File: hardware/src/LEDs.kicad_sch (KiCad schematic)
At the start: 0 parts

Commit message: Add: LEDs to the schematic
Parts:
- added R601: 220R, symbol Device:R
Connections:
- new net LED11-1/D_{IN}: R601.1
- new net LED_{IN}: R601.2
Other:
- added sheet LED11-1 (LEDx11.kicad_sch)
- added sheet LED11-10 (LEDx11.kicad_sch)
- added sheet LED11-2 (LEDx11.kicad_sch)
- added sheet LED11-3 (LEDx11.kicad_sch)
- added sheet LED11-4 (LEDx11.kicad_sch)
- added sheet LED11-5 (LEDx11.kicad_sch)
- added sheet LED11-6 (LEDx11.kicad_sch)
- added sheet LED11-7 (LEDx11.kicad_sch)
- added sheet LED11-8 (LEDx11.kicad_sch)
- added sheet LED11-9 (LEDx11.kicad_sch)

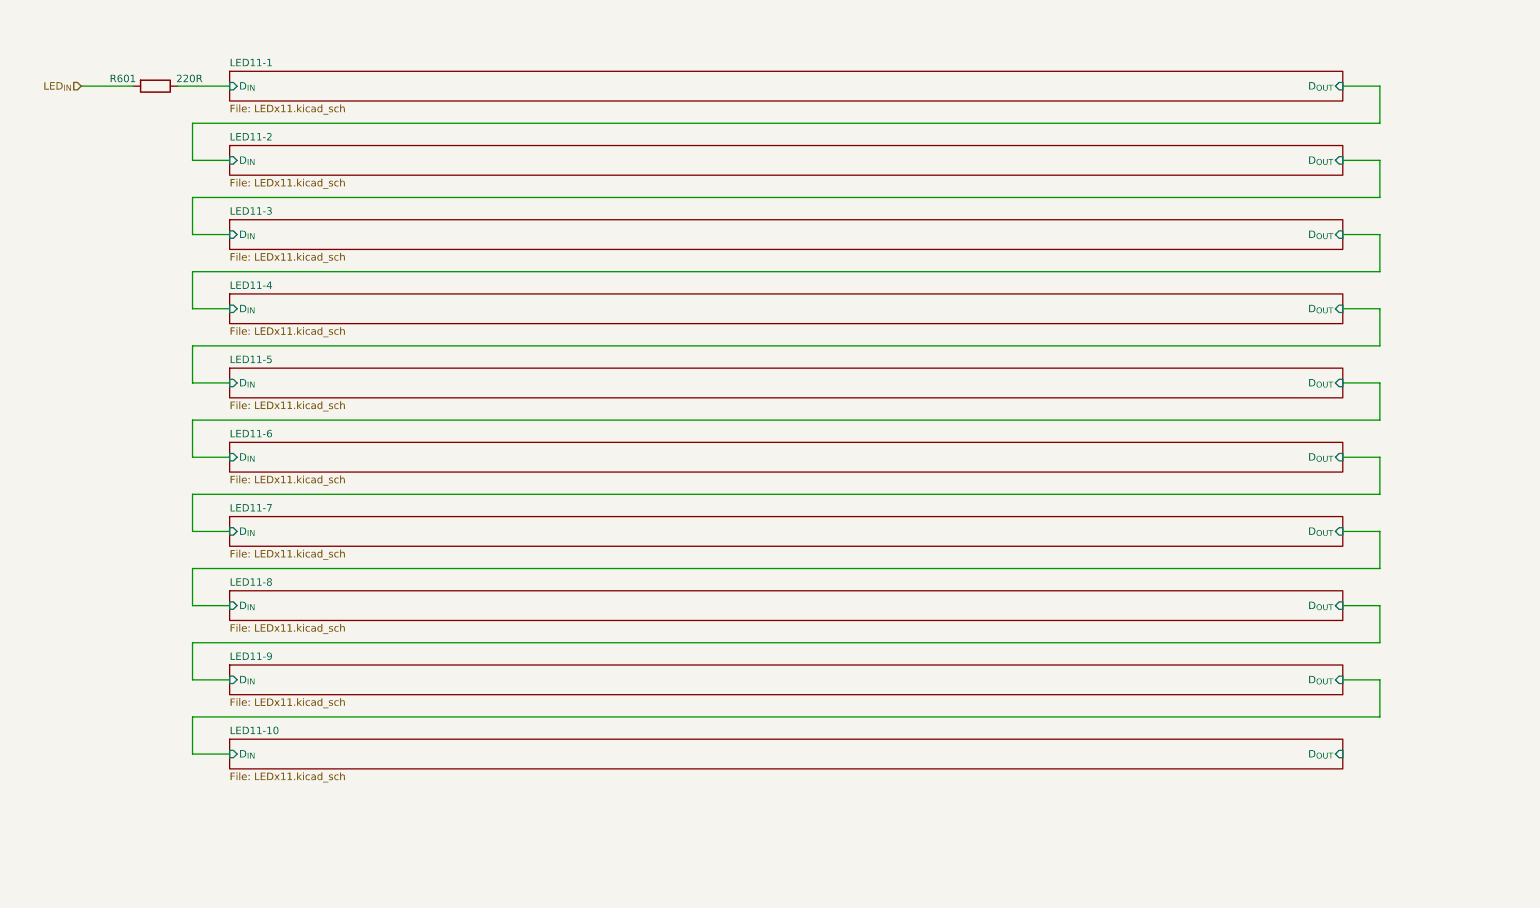
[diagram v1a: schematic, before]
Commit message: Add: RTC schematic
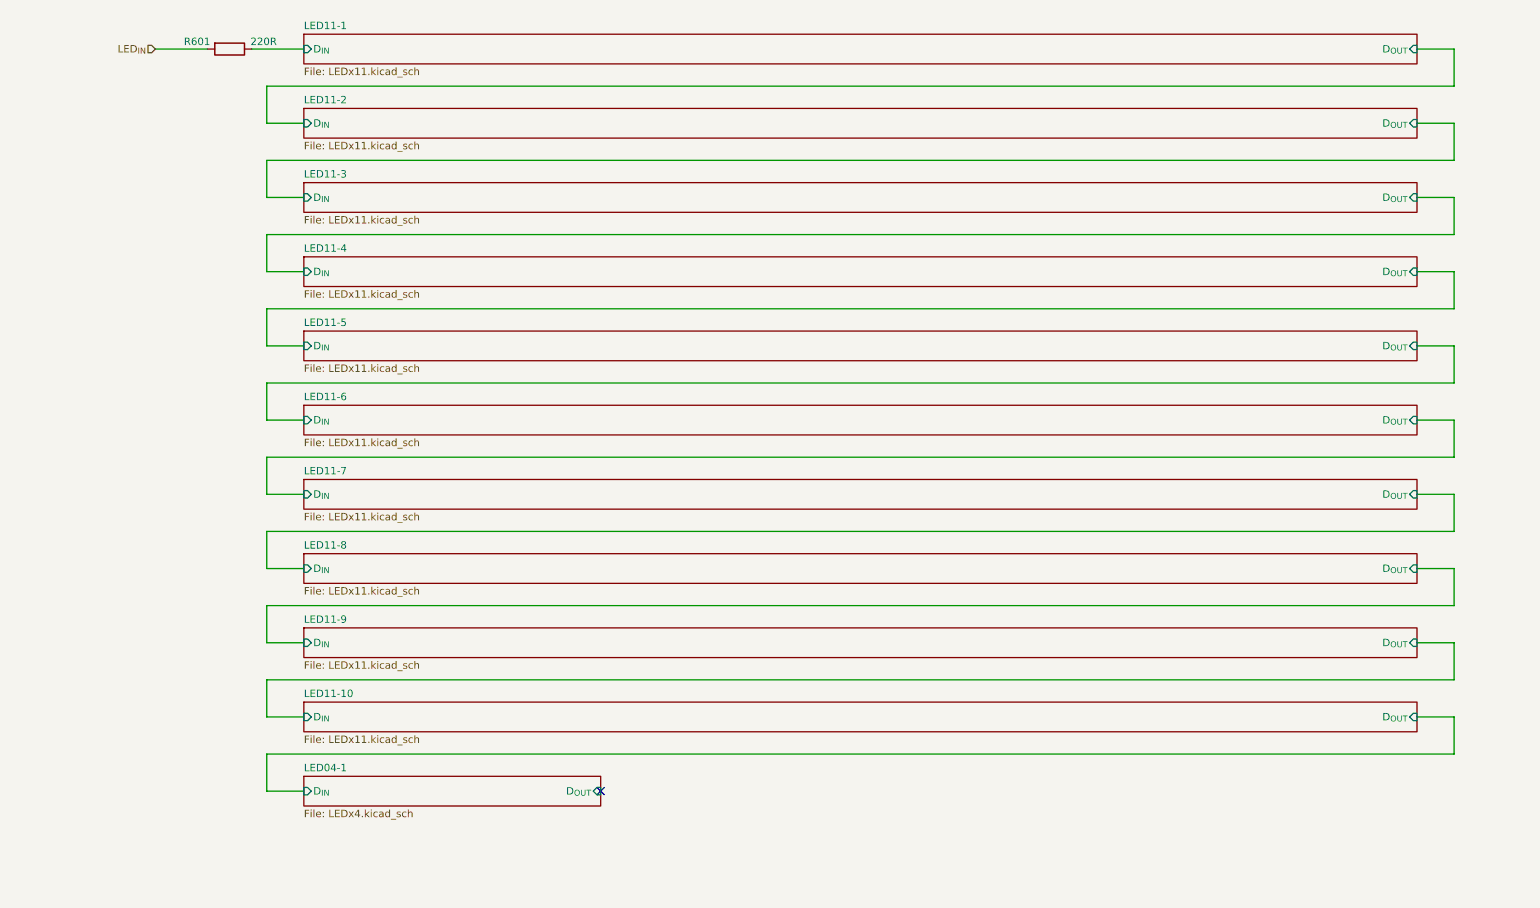
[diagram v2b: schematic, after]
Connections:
- no-connect marks 0 -> 1
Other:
- added sheet LED04-1 (LEDx4.kicad_sch)
- moved on the sheet: R601

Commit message: Add: Level Shifter +3V3 to +5V
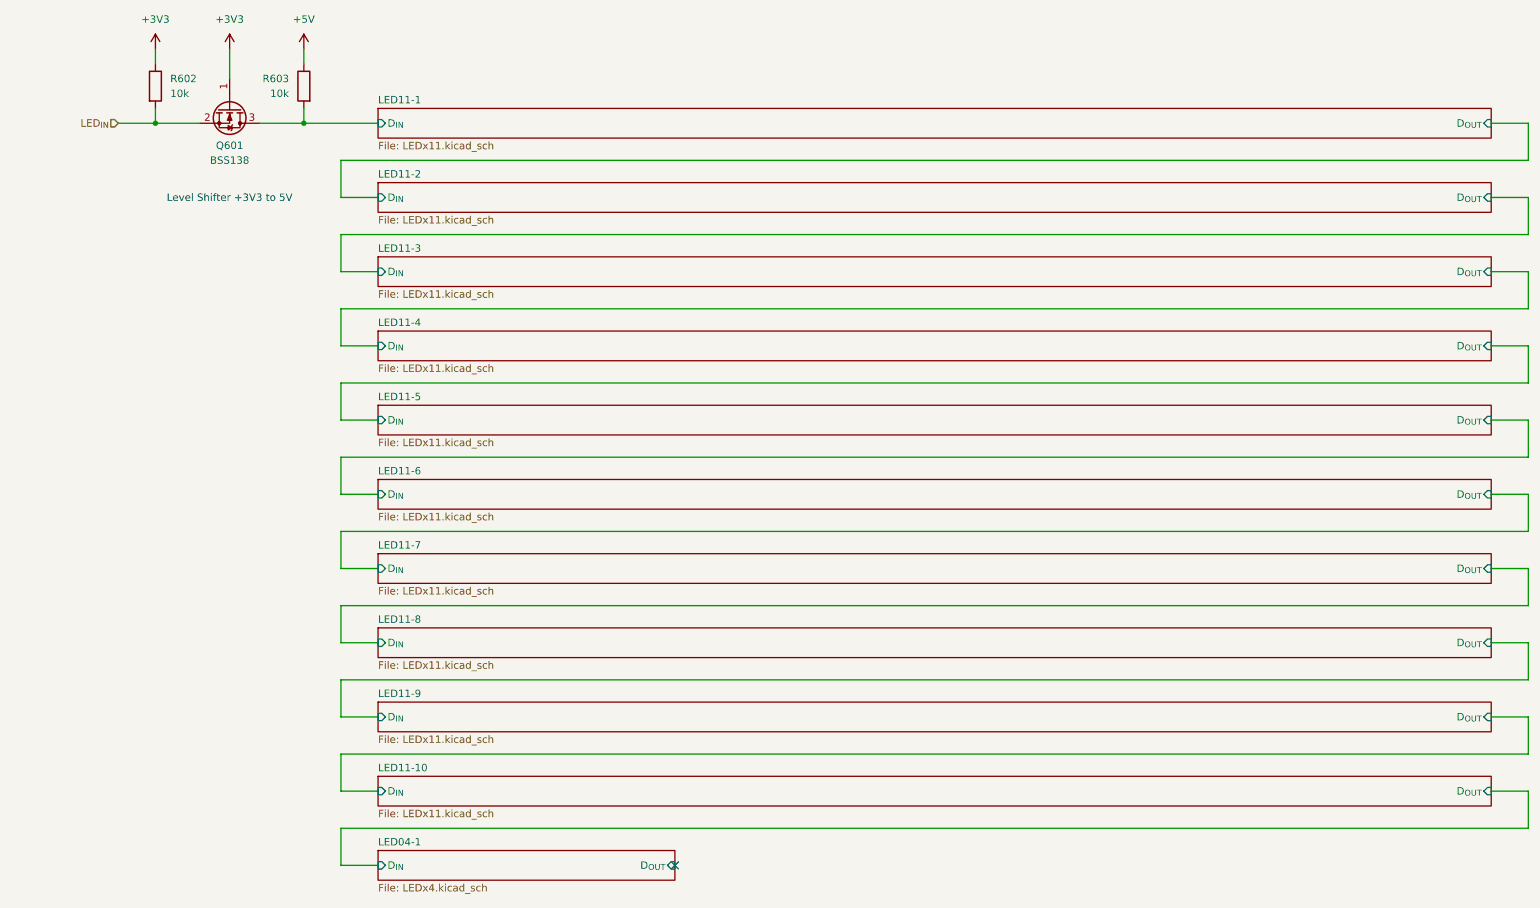
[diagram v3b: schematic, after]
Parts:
- removed R601: 220R, symbol Device:R
- added Q601: BSS138, Package_TO_SOT_SMD:SOT-23, symbol Transistor_FET:BSS138
- added R602, R603: 10k, symbol Device:R
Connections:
- net LED11-1/D_{IN}: now also Q601.3 (D), R603.2
- net LED_{IN}: now also Q601.2 (S), R602.2
- new net +3V3: Q601.1 (G), R602.1
- new net +5V: R603.1
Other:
- note added: "Level Shifter +3V3 to 5V"

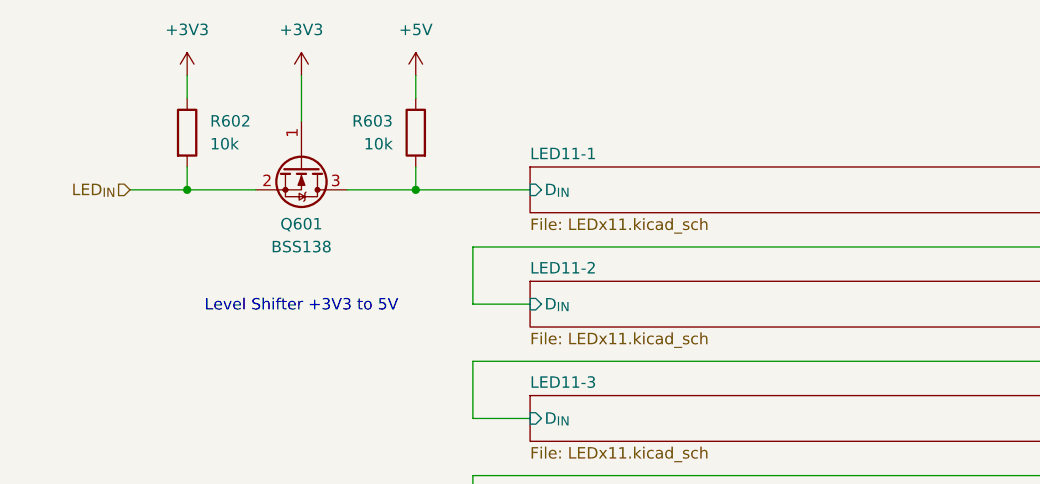
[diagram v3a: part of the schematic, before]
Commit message: Add: Text Headers to the indidual schematic regions
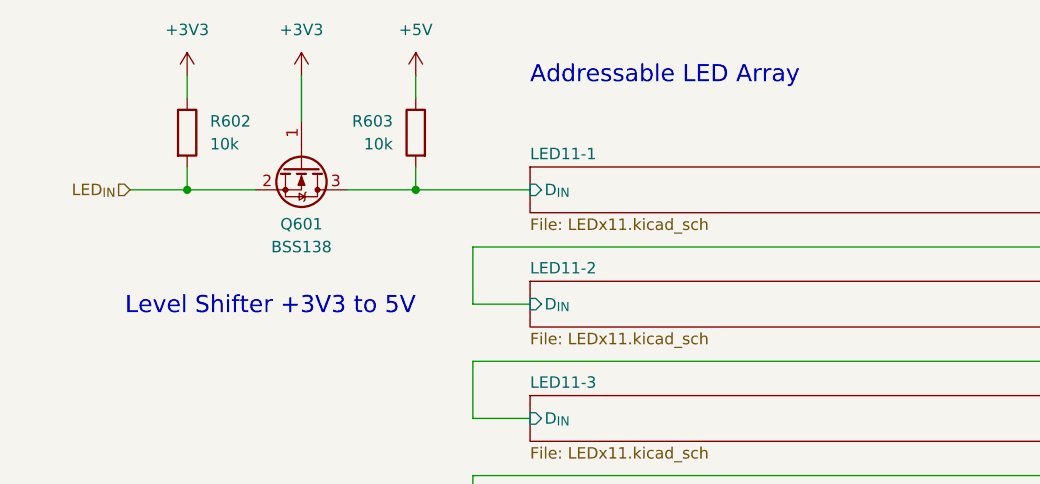
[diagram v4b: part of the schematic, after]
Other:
- note added: "Addressable LED Array"
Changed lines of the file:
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@@
 	(text "Level Shifter +3V3 to 5V"
 		(exclude_from_sim no)
-		(at 50.8 51.054 0)
+		(at 63.5 51.054 0)
 		(effects
 			(font
-				(size 1.27 1.27)
+				(size 1.905 1.905)
 			)
+			(justify right)
 		)
 	)
+	(text "Addressable LED Array"
+		(exclude_from_sim no)
+		(at 76.2 25.4 0)
+		(effects
+			(font
+				(size 1.905 1.905)
+			)
+			(justify left)
+		)
+	)
